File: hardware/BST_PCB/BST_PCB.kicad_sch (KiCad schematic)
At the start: 6 parts

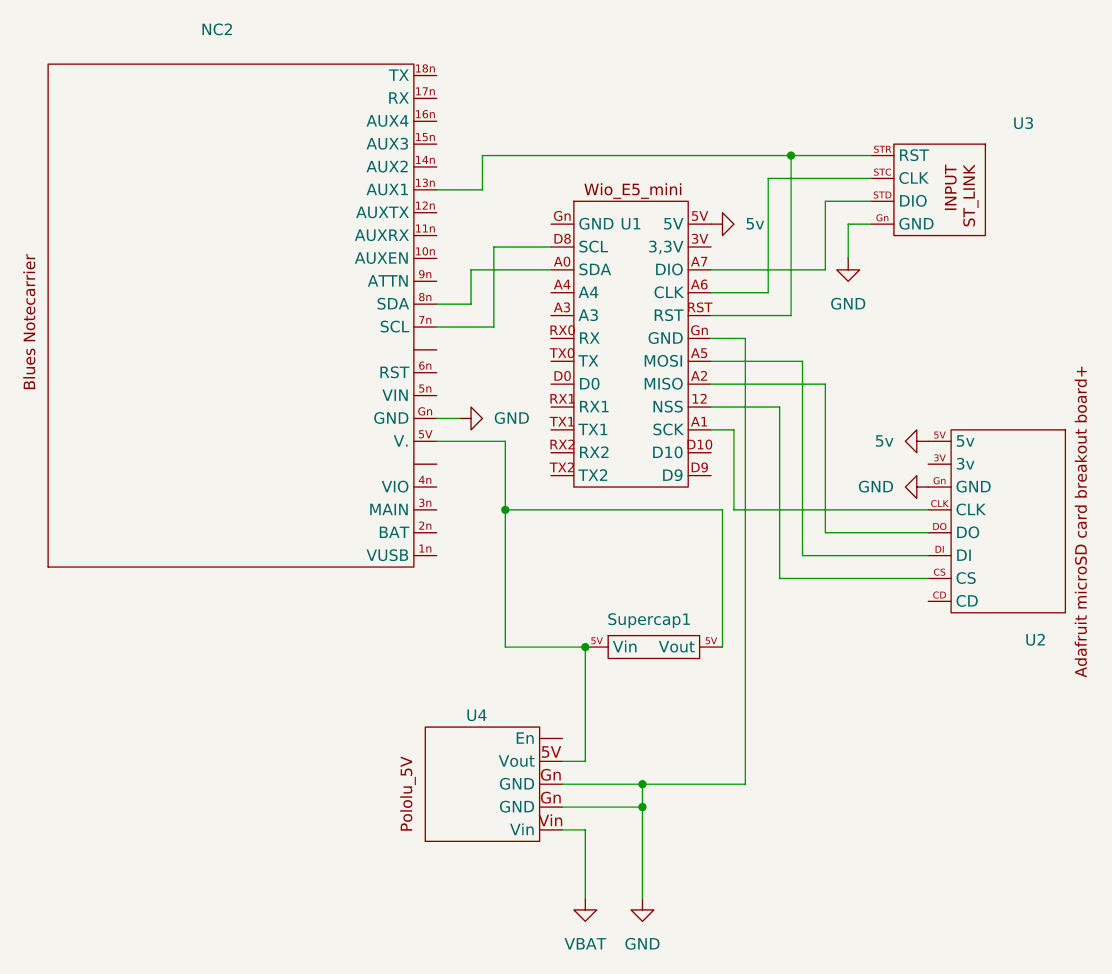
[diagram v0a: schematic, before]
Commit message: Fixed schematic bugs
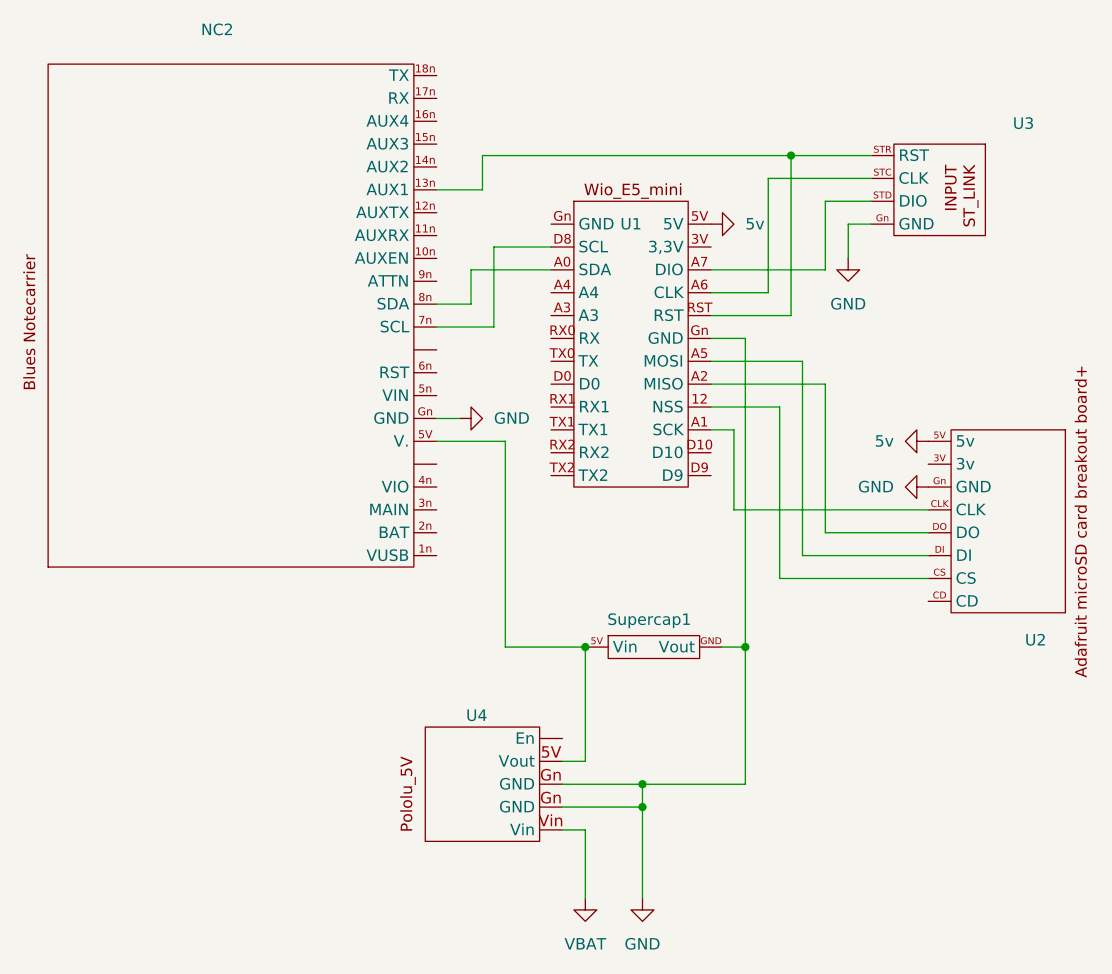
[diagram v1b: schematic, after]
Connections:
- net GND: now also Supercap1.GND (Vout)
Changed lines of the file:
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@@
-	)
-	(junction
-		(at 72.39 66.04)
-		(diameter 0)
-		(color 0 0 0 0)
 	)
 	(junction
@@
 	)
 	(junction
+		(at 99.06 81.28)
+		(diameter 0)
+		(color 0 0 0 1)
+	)
+	(junction
 		(at 81.28 81.28)
 		(diameter 0)
@@
 	(wire
 		(pts
-			(xy 72.39 58.42) (xy 72.39 66.04)
-		)
-		(stroke
-			(width 0)
-			(type default)
-		)
-	)
-	(wire
-		(pts
 			(xy 71.12 36.83) (xy 71.12 45.72)
 		)
@@
 	(wire
 		(pts
-			(xy 96.52 81.28) (xy 96.52 66.04)
-		)
-		(stroke
-			(width 0)
-			(type default)
-		)
-	)
-	(wire
-		(pts
 			(xy 102.87 73.66) (xy 102.87 54.61)
 		)
@@
 	(wire
 		(pts
-			(xy 99.06 46.99) (xy 99.06 96.52)
+			(xy 99.06 46.99) (xy 99.06 81.28)
 		)
 		(stroke
@@
 	(wire
 		(pts
+			(xy 96.52 81.28) (xy 99.06 81.28)
+		)
+		(stroke
+			(width 0)
+			(type default)
+			(color 0 0 0 1)
+		)
+	)
+	(wire
+		(pts
 			(xy 81.28 93.98) (xy 81.28 81.28)
 		)
@@
 	(wire
 		(pts
-			(xy 96.52 66.04) (xy 72.39 66.04)
-		)
-		(stroke
-			(width 0)
-			(type default)
-		)
-	)
-	(wire
-		(pts
 			(xy 105.41 49.53) (xy 95.25 49.53)
 		)
@@
 	(wire
 		(pts
-			(xy 72.39 66.04) (xy 72.39 81.28)
+			(xy 72.39 58.42) (xy 72.39 81.28)
 		)
 		(stroke
@@
 			(width 0)
 			(type default)
+		)
+	)
+	(wire
+		(pts
+			(xy 99.06 81.28) (xy 99.06 96.52)
+		)
+		(stroke
+			(width 0)
+			(type default)
+			(color 0 0 0 1)
 		)
 	)
@@
 		)
 		(instances
-			(project ""
+			(project "BST_PCB"
 				(path "/35351956-19cf-4c13-9aee-d5913c862f0e"
 					(reference "U1")
@@
 		)
 		(instances
-			(project ""
+			(project "BST_PCB"
 				(path "/35351956-19cf-4c13-9aee-d5913c862f0e"
 					(reference "#PWR01")
@@
 		)
 		(instances
-			(project ""
+			(project "BST_PCB"
 				(path "/35351956-19cf-4c13-9aee-d5913c862f0e"
 					(reference "NC2")
@@
 		(pin "5V"
 		)
-		(pin "5V"
+		(pin "GND"
 		)
 		(instances
-			(project ""
+			(project "BST_PCB"
 				(path "/35351956-19cf-4c13-9aee-d5913c862f0e"
 					(reference "Supercap1")
@@
 		)
 		(instances
-			(project ""
+			(project "BST_PCB"
 				(path "/35351956-19cf-4c13-9aee-d5913c862f0e"
 					(reference "U3")
@@
 		)
 		(instances
-			(project ""
+			(project "BST_PCB"
 				(path "/35351956-19cf-4c13-9aee-d5913c862f0e"
 					(reference "U2")
@@
 		)
 		(instances
-			(project ""
+			(project "BST_PCB"
 				(path "/35351956-19cf-4c13-9aee-d5913c862f0e"
 					(reference "U4")
